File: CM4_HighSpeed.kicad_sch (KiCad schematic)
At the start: 13 parts, among them J10 690-019-298-412, J15 Conn_01x22_Female, J16 Conn_01x22_Female, J22 690-019-298-412, J4 Conn_01x22_Female, J5 Conn_01x22_Female, J6 THD-02-R, U12 RT9742SNGV

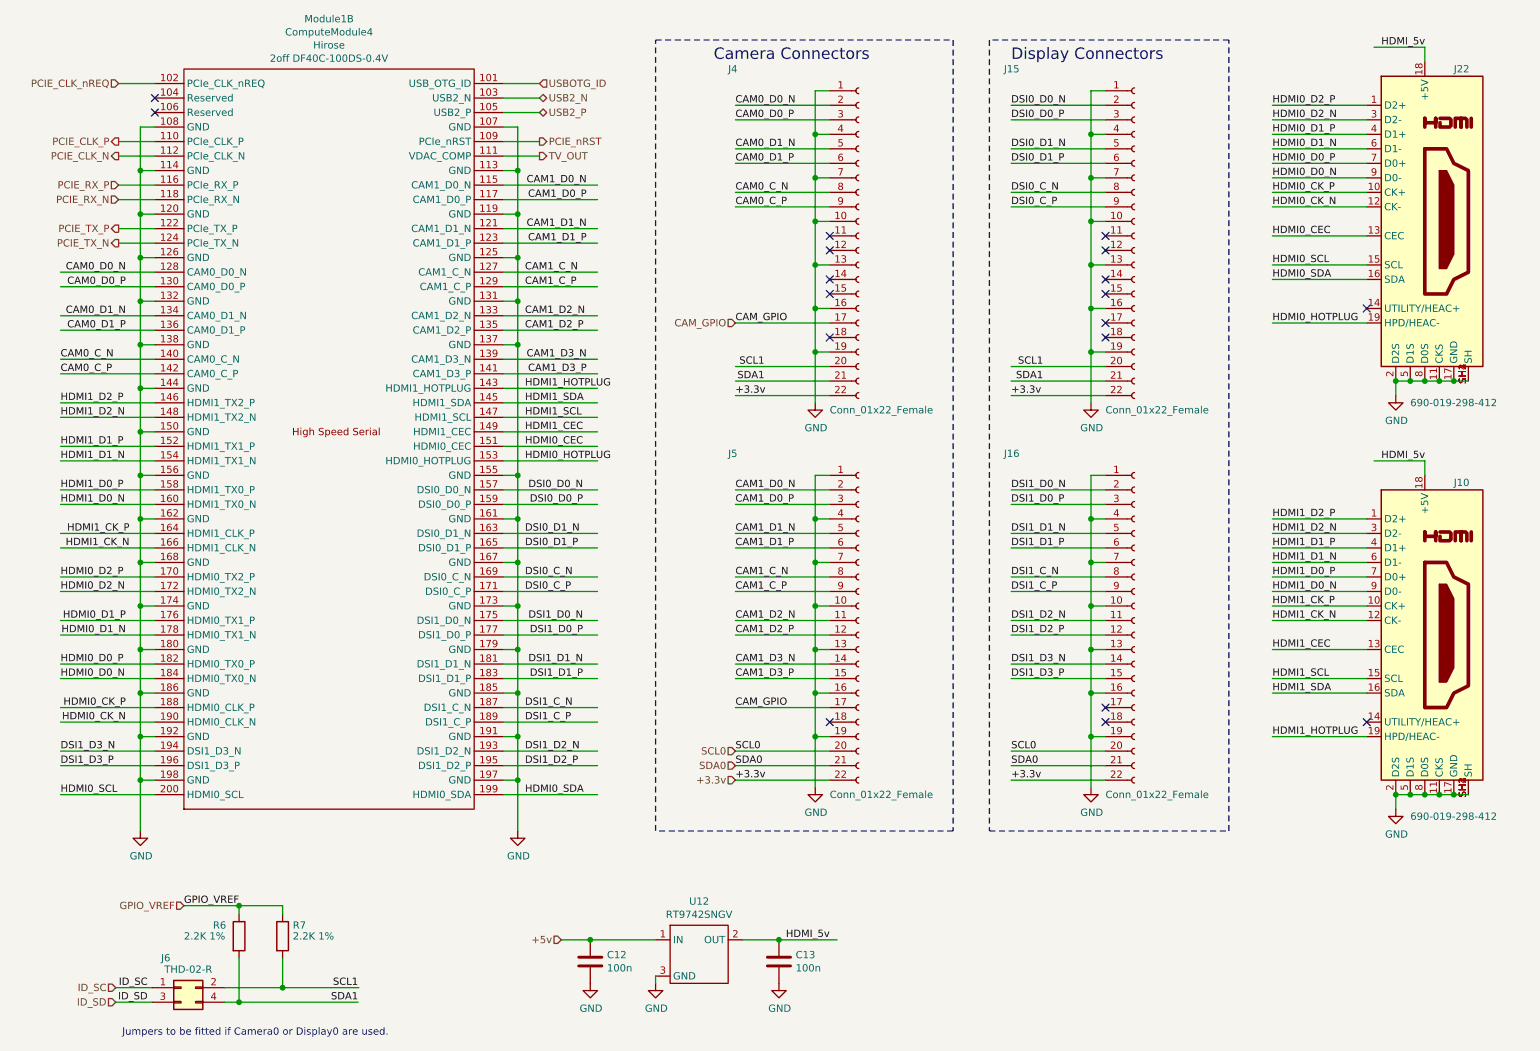
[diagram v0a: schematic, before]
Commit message: Removing unneeded items
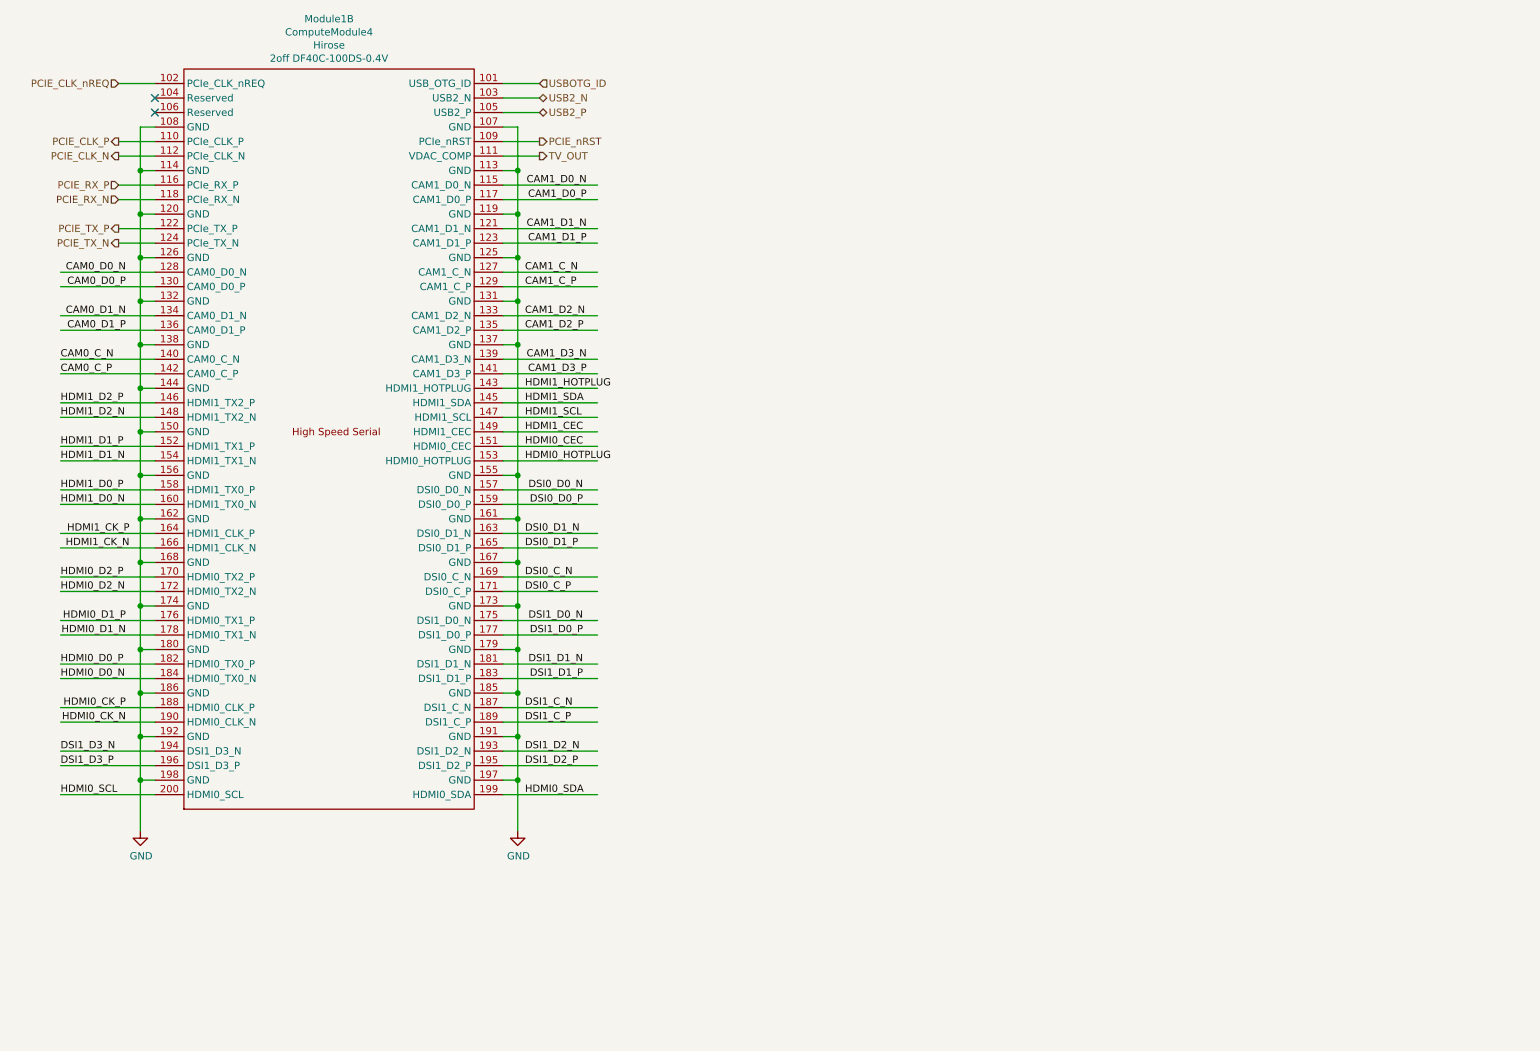
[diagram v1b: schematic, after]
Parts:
- removed C12, C13: 100n, Capacitor_SMD:C_0402_1005Metric, symbol Device:C
- removed J10, J22: 690-019-298-412, CM4IO:EDAC 690-019-298-412, symbol CM4IO:HDMI_A_1.4
- removed J15, J16, J4, J5: Conn_01x22_Female, CM4IO:Hirose_FH12-22S-0.5SH_1x22-1MP_P0.50mm_Horizontal, symbol Connector:Conn_01x22_Female
- removed J6: THD-02-R, Connector_PinHeader_2.54mm:PinHeader_2x02_P2.54mm_Vertical, symbol Connector_Generic:Conn_02x02_Odd_Even
- removed R6, R7: 2.2K 1%, Resistor_SMD:R_0402_1005Metric, symbol Device:R
- removed U12: RT9742SNGV, Package_TO_SOT_SMD:SOT-23, symbol CM4IO:RT9742SNGV
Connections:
- no-connect marks 18 -> 2
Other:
- note removed: "Camera Connectors"
- note removed: "Display Connectors"
- note removed: "Jumpers to be fitted if Camera0 or Display0 are used."
